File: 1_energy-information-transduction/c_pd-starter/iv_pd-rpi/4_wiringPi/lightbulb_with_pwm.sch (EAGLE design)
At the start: 3 parts, among them Q1 2N3904

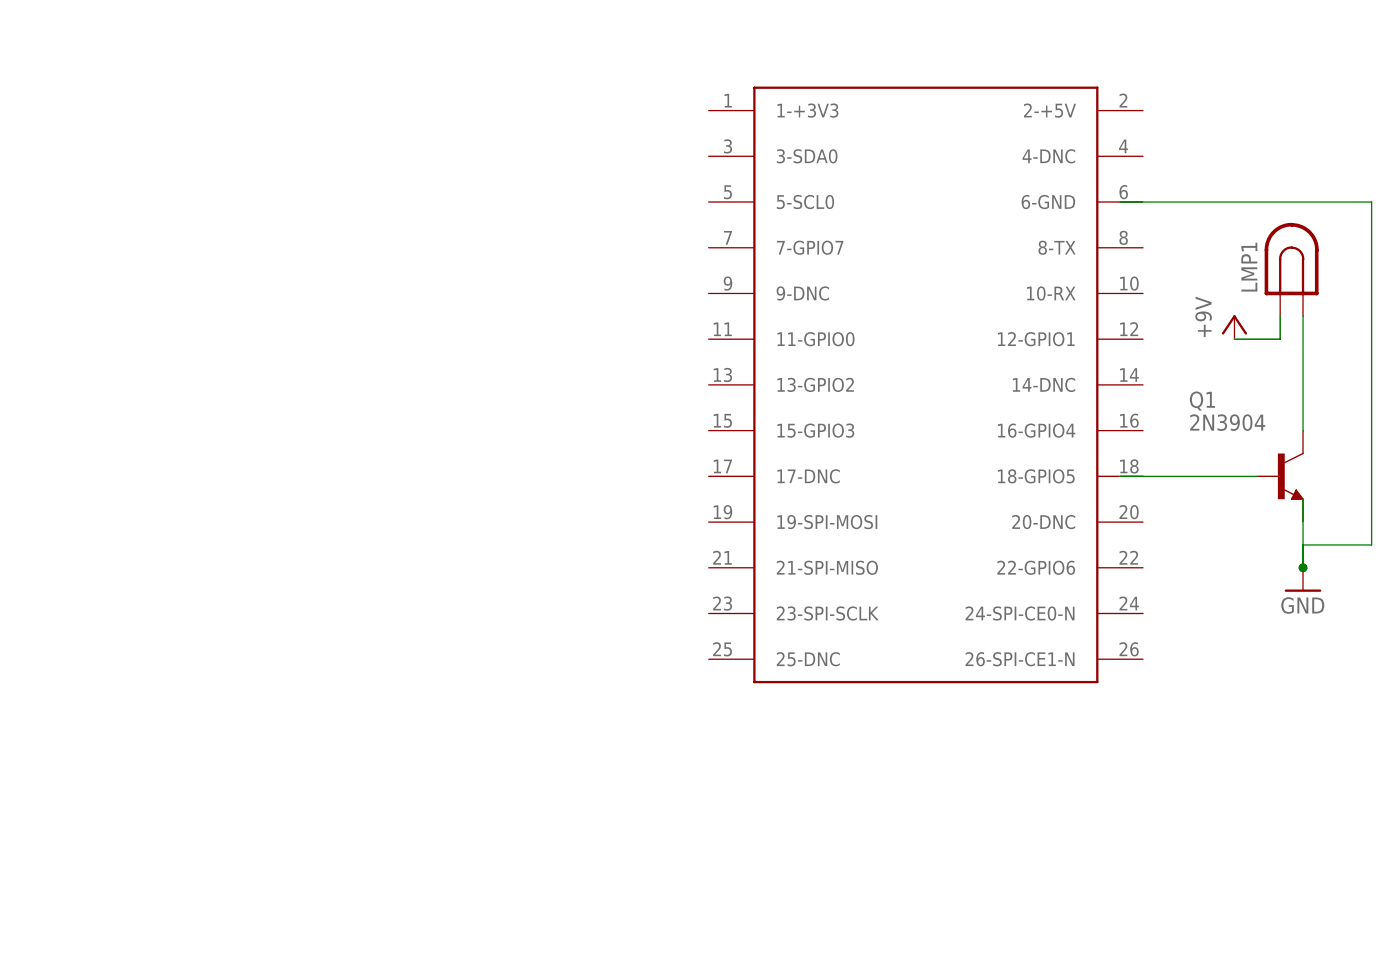
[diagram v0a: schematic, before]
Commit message: Add diagrams for first WiringPi examples.
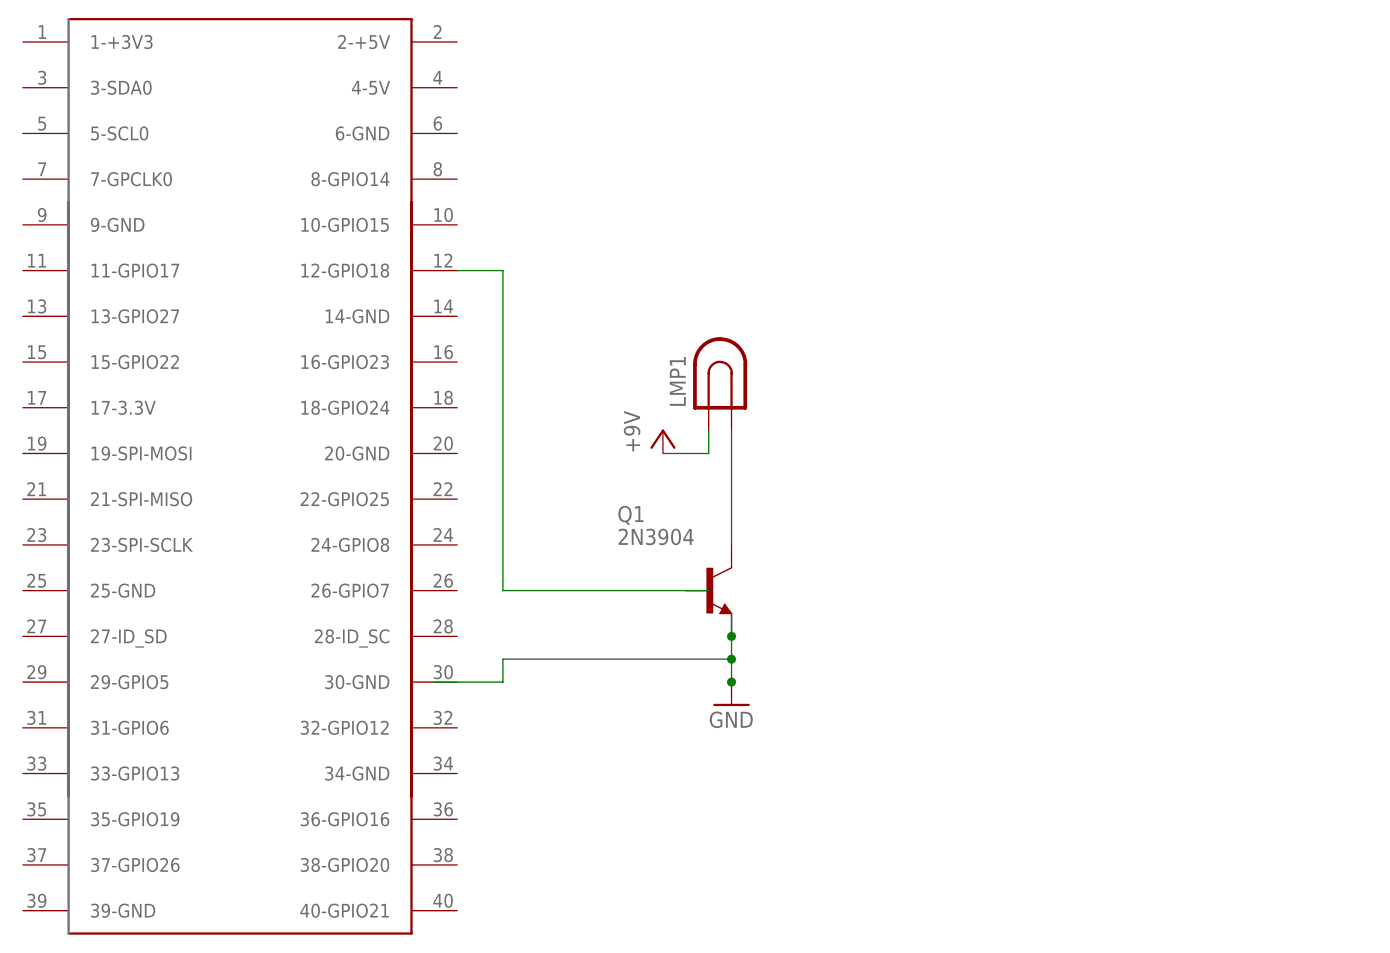
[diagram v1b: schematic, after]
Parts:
- removed U$1: RASPBERRY-PI, RaspberryPi:RASPBERRY-PI
- added U$2: RASPBERRY-PI, aliEagleLib:RASPBERRY-PI
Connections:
- new net GND: Q1.E
- net N$1: now also U$2.12-GPIO18; no longer Q1.B
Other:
- moved on the sheet: LMP1, Q1
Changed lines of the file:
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@@
 <layer number="48" name="Document" color="7" fill="1" visible="no" active="no"/>
 <layer number="49" name="Reference" color="7" fill="1" visible="no" active="no"/>
+<layer number="50" name="dxf" color="7" fill="1" visible="no" active="no"/>
 <layer number="51" name="tDocu" color="14" fill="1" visible="no" active="no"/>
 <layer number="52" name="bDocu" color="7" fill="1" visible="no" active="no"/>
+<layer number="53" name="tGND_GNDA" color="7" fill="9" visible="no" active="no"/>
+<layer number="54" name="bGND_GNDA" color="1" fill="9" visible="no" active="no"/>
+<layer number="56" name="wert" color="7" fill="1" visible="no" active="no"/>
 <layer number="90" name="Modules" color="5" fill="1" visible="yes" active="yes"/>
 <layer number="91" name="Nets" color="2" fill="1" visible="yes" active="yes"/>
@@
 <layer number="97" name="Info" color="7" fill="1" visible="yes" active="yes"/>
 <layer number="98" name="Guide" color="6" fill="1" visible="yes" active="yes"/>
+<layer number="100" name="Muster" color="7" fill="1" visible="no" active="no"/>
+<layer number="101" name="Patch_Top" color="12" fill="4" visible="no" active="yes"/>
+<layer number="102" name="Vscore" color="7" fill="1" visible="no" active="yes"/>
+<layer number="103" name="tMap" color="7" fill="1" visible="no" active="yes"/>
+<layer number="104" name="Name" color="16" fill="1" visible="yes" active="yes"/>
+<layer number="105" name="tPlate" color="7" fill="1" visible="yes" active="yes"/>
+<layer number="106" name="bPlate" color="7" fill="1" visible="yes" active="yes"/>
+<layer number="107" name="Crop" color="7" fill="1" visible="yes" active="yes"/>
+<layer number="116" name="Patch_BOT" color="9" fill="4" visible="no" active="yes"/>
+<layer number="121" name="_tsilk" color="7" fill="1" visible="no" active="yes"/>
+<layer number="122" name="_bsilk" color="7" fill="1" visible="no" active="yes"/>
+<layer number="125" name="_tNames" color="7" fill="1" visible="yes" active="yes"/>
+<layer number="144" name="Drill_legend" color="7" fill="1" visible="no" active="yes"/>
+<layer number="151" name="HeatSink" color="7" fill="1" visible="no" active="yes"/>
+<layer number="199" name="Contour" color="7" fill="1" visible="yes" active="yes"/>
+<layer number="200" name="200bmp" color="1" fill="10" visible="no" active="yes"/>
+<layer number="201" name="201bmp" color="2" fill="10" visible="no" active="yes"/>
+<layer number="202" name="202bmp" color="3" fill="10" visible="no" active="yes"/>
+<layer number="203" name="203bmp" color="4" fill="10" visible="no" active="yes"/>
+<layer number="204" name="204bmp" color="5" fill="10" visible="no" active="yes"/>
+<layer number="205" name="205bmp" color="6" fill="10" visible="no" active="yes"/>
+<layer number="206" name="206bmp" color="7" fill="10" visible="no" active="yes"/>
+<layer number="207" name="207bmp" color="8" fill="10" visible="no" active="yes"/>
+<layer number="208" name="208bmp" color="9" fill="10" visible="no" active="yes"/>
+<layer number="209" name="209bmp" color="7" fill="1" visible="no" active="yes"/>
+<layer number="210" name="210bmp" color="7" fill="1" visible="no" active="yes"/>
+<layer number="211" name="211bmp" color="7" fill="1" visible="no" active="yes"/>
+<layer number="212" name="212bmp" color="7" fill="1" visible="no" active="yes"/>
+<layer number="213" name="213bmp" color="7" fill="1" visible="no" active="yes"/>
+<layer number="214" name="214bmp" color="7" fill="1" visible="no" active="yes"/>
+<layer number="215" name="215bmp" color="7" fill="1" visible="no" active="yes"/>
+<layer number="216" name="216bmp" color="7" fill="1" visible="no" active="yes"/>
+<layer number="217" name="217bmp" color="18" fill="1" visible="no" active="no"/>
+<layer number="218" name="218bmp" color="19" fill="1" visible="no" active="no"/>
+<layer number="219" name="219bmp" color="20" fill="1" visible="no" active="no"/>
+<layer number="220" name="220bmp" color="21" fill="1" visible="no" active="no"/>
+<layer number="221" name="221bmp" color="22" fill="1" visible="no" active="no"/>
+<layer number="222" name="222bmp" color="23" fill="1" visible="no" active="no"/>
+<layer number="223" name="223bmp" color="24" fill="1" visible="no" active="no"/>
+<layer number="224" name="224bmp" color="25" fill="1" visible="no" active="no"/>
+<layer number="250" name="Descript" color="3" fill="1" visible="no" active="no"/>
+<layer number="251" name="SMDround" color="12" fill="11" visible="no" active="no"/>
+<layer number="254" name="cooling" color="7" fill="1" visible="no" active="yes"/>
 </layers>
 <schematic xreflabel="%F%N/%S.%C%R" xrefpart="/%S.%C%R">
@@
 </classes>
 <parts>
-<part name="U$1" library="RaspberryPi" deviceset="RASPBERRY-PI" device=""/>
 <part name="Q1" library="transistor-npn" deviceset="2N3904" device=""/>
 <part name="P+1" library="supply1" deviceset="VCC" device="" value="+9V"/>
 <part name="GND1" library="supply1" deviceset="GND" device=""/>
 <part name="LMP1" library="special" deviceset="LAMP" device=""/>
+<part name="U$2" library="aliEagleLib" deviceset="RASPBERRY-PI" device=""/>
 </parts>
 <sheets>
@@
 </plain>
 <instances>
-<instance part="U$1" gate="G$1" x="43.18" y="27.94"/>
-<instance part="Q1" gate="G1" x="86.36" y="38.1"/>
-<instance part="P+1" gate="VCC" x="81.28" y="55.88"/>
-<instance part="GND1" gate="1" x="88.9" y="25.4"/>
-<instance part="LMP1" gate="G$1" x="86.36" y="60.96"/>
+<instance part="Q1" gate="G1" x="22.86" y="25.4"/>
+<instance part="P+1" gate="VCC" x="17.78" y="43.18"/>
+<instance part="GND1" gate="1" x="25.4" y="12.7"/>
+<instance part="LMP1" gate="G$1" x="22.86" y="48.26"/>
+<instance part="U$2" gate="G$1" x="-27.94" y="33.02"/>
 </instances>
 <busses>
 </busses>
 <nets>
-<net name="N$1" class="0">
-<segment>
-<pinref part="Q1" gate="G1" pin="B"/>
-<wire x1="68.58" y1="38.1" x2="83.82" y2="38.1" width="0.1524" layer="91"/>
-</segment>
-</net>
 <net name="VCC" class="0">
 <segment>
 <pinref part="P+1" gate="VCC" pin="VCC"/>
 <pinref part="LMP1" gate="G$1" pin="1"/>
-<wire x1="81.28" y1="53.34" x2="86.36" y2="53.34" width="0.1524" layer="91"/>
-<wire x1="86.36" y1="53.34" x2="86.36" y2="55.88" width="0.1524" layer="91"/>
+<wire x1="17.78" y1="40.64" x2="22.86" y2="40.64" width="0.1524" layer="91"/>
+<wire x1="22.86" y1="40.64" x2="22.86" y2="43.18" width="0.1524" layer="91"/>
 </segment>
 </net>
@@
 <pinref part="LMP1" gate="G$1" pin="2"/>
 <pinref part="Q1" gate="G1" pin="C"/>
-<wire x1="88.9" y1="55.88" x2="88.9" y2="43.18" width="0.1524" layer="91"/>
+<wire x1="25.4" y1="43.18" x2="25.4" y2="30.48" width="0.1524" layer="91"/>
 </segment>
 </net>
@@
 <segment>
 <pinref part="GND1" gate="1" pin="GND"/>
-<wire x1="88.9" y1="35.56" x2="88.9" y2="27.94" width="0.1524" layer="91"/>
-<wire x1="68.58" y1="68.58" x2="96.52" y2="68.58" width="0.1524" layer="91"/>
-<wire x1="96.52" y1="68.58" x2="96.52" y2="30.48" width="0.1524" layer="91"/>
-<wire x1="96.52" y1="30.48" x2="88.9" y2="30.48" width="0.1524" layer="91"/>
-<wire x1="88.9" y1="30.48" x2="88.9" y2="27.94" width="0.1524" layer="91"/>
-<junction x="88.9" y="27.94"/>
+<wire x1="25.4" y1="22.86" x2="25.4" y2="20.32" width="0.1524" layer="91"/>
+<pinref part="Q1" gate="G1" pin="E"/>
+<junction x="25.4" y="20.32"/>
+<wire x1="25.4" y1="20.32" x2="25.4" y2="17.78" width="0.1524" layer="91"/>
+<junction x="25.4" y="15.24"/>
+<wire x1="25.4" y1="17.78" x2="25.4" y2="15.24" width="0.1524" layer="91"/>
+<wire x1="25.4" y1="17.78" x2="0" y2="17.78" width="0.1524" layer="91"/>
+<wire x1="0" y1="17.78" x2="0" y2="15.24" width="0.1524" layer="91"/>
+<junction x="25.4" y="17.78"/>
+<wire x1="0" y1="15.24" x2="-7.62" y2="15.24" width="0.1524" layer="91"/>
 </segment>
 </net>
+<net name="N$1" class="0">
+<segment>
+<wire x1="22.86" y1="25.4" x2="0" y2="25.4" width="0.1524" layer="91"/>
+<wire x1="0" y1="25.4" x2="0" y2="60.96" width="0.1524" layer="91"/>
+<pinref part="U$2" gate="G$1" pin="12-GPIO18"/>
+<wire x1="0" y1="60.96" x2="-5.08" y2="60.96" width="0.1524" layer="91"/>
+</segment>
+</net>
